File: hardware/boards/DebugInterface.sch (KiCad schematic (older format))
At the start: 1 part

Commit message: Updated part mfr and added the proper part numbers
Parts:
- U?: MFR (none) -> Lattice; MPN (none) -> LFE5UM5G-85F-8BG381I
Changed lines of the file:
@@
 $Descr A4 11693 8268
 encoding utf-8
-Sheet 9 11
+Sheet 8 11
 Title ""
 Date ""
@@
 F 2 "" H 4500 3300 50  0001 C CNN
 F 3 "" H 4500 3300 50  0001 C CNN
+F 4 "Lattice" H 5850 3150 50  0001 C CNN "MFR"
+F 5 "LFE5UM5G-85F-8BG381I" H 5850 3150 50  0001 C CNN "MPN"
 	5    5850 3150
 	1    0    0    -1

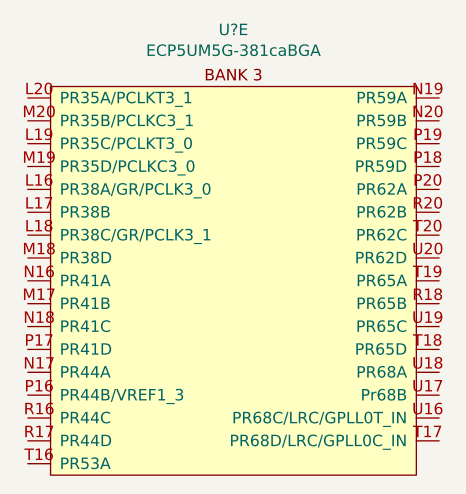
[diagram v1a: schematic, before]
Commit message: Did some annotation and fixed the FPGA bank that was accidentally labled as the cypress part
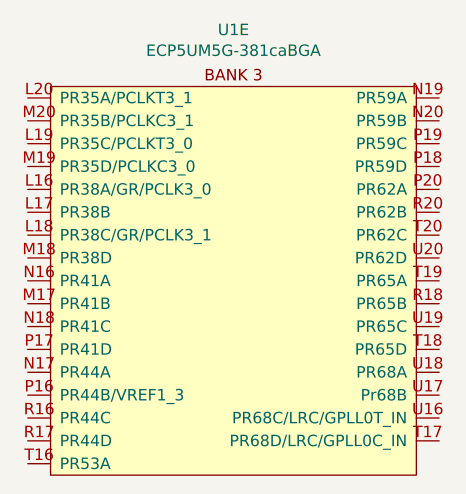
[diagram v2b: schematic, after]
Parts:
- U1: renamed from U?; footprint (none) -> lethalbit:318caBGA
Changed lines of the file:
@@
 $EndDescr
 $Comp
-L lethalbit:ECP5UM5G-381caBGA U?
+L lethalbit:ECP5UM5G-381caBGA U1
 U 5 1 5F210C09
 P 5850 3150
-F 0 "U?" H 5850 3498 50  0000 C CNN
+F 0 "U1" H 5850 3498 50  0000 C CNN
 F 1 "ECP5UM5G-381caBGA" H 5850 3407 50  0000 C CNN
-F 2 "" H 4500 3300 50  0001 C CNN
+F 2 "lethalbit:318caBGA" H 4500 3300 50  0001 C CNN
 F 3 "" H 4500 3300 50  0001 C CNN
 F 4 "Lattice" H 5850 3150 50  0001 C CNN "MFR"

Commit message: Some more mist schematic edits
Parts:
- U1: DIGIKEY_PN (none) -> 220-2112-ND
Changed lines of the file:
@@
 F 4 "Lattice" H 5850 3150 50  0001 C CNN "MFR"
 F 5 "LFE5UM5G-85F-8BG381I" H 5850 3150 50  0001 C CNN "MPN"
+F 6 "220-2112-ND" H 5850 3150 50  0001 C CNN "DIGIKEY_PN"
 	5    5850 3150
 	1    0    0    -1

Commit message: Some strugglebusting on getting the ERC errors cleaned up a bit
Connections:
- no-connect marks 0 -> 33
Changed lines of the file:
@@
 	1    0    0    -1
 $EndComp
+NoConn ~ 4950 3100
+NoConn ~ 4950 3200
+NoConn ~ 4950 3300
+NoConn ~ 4950 3400
+NoConn ~ 4950 3500
+NoConn ~ 4950 3600
+NoConn ~ 4950 3700
+NoConn ~ 4950 3800
+NoConn ~ 4950 3900
+NoConn ~ 4950 4000
+NoConn ~ 4950 4100
+NoConn ~ 4950 4200
+NoConn ~ 4950 4300
+NoConn ~ 4950 4400
+NoConn ~ 4950 4500
+NoConn ~ 4950 4600
+NoConn ~ 4950 4700
+NoConn ~ 6750 4600
+NoConn ~ 6750 4500
+NoConn ~ 6750 4400
+NoConn ~ 6750 4300
+NoConn ~ 6750 4200
+NoConn ~ 6750 4100
+NoConn ~ 6750 4000
+NoConn ~ 6750 3900
+NoConn ~ 6750 3800
+NoConn ~ 6750 3700
+NoConn ~ 6750 3600
+NoConn ~ 6750 3500
+NoConn ~ 6750 3400
+NoConn ~ 6750 3300
+NoConn ~ 6750 3200
+NoConn ~ 6750 3100
 $EndSCHEMATC
